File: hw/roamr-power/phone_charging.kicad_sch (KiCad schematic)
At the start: 0 parts

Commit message: reorganizing to roamr-power
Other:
- title: (none) -> ROAMR power board
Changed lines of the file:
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@@
 	(generator_version "9.0")
 	(paper "USLetter")
+	(title_block
+		(title "ROAMR power board")
+		(date "2026-01-18")
+		(rev "1.0")
+	)
 	(text "current limiter load switch here"
 		(exclude_from_sim no)

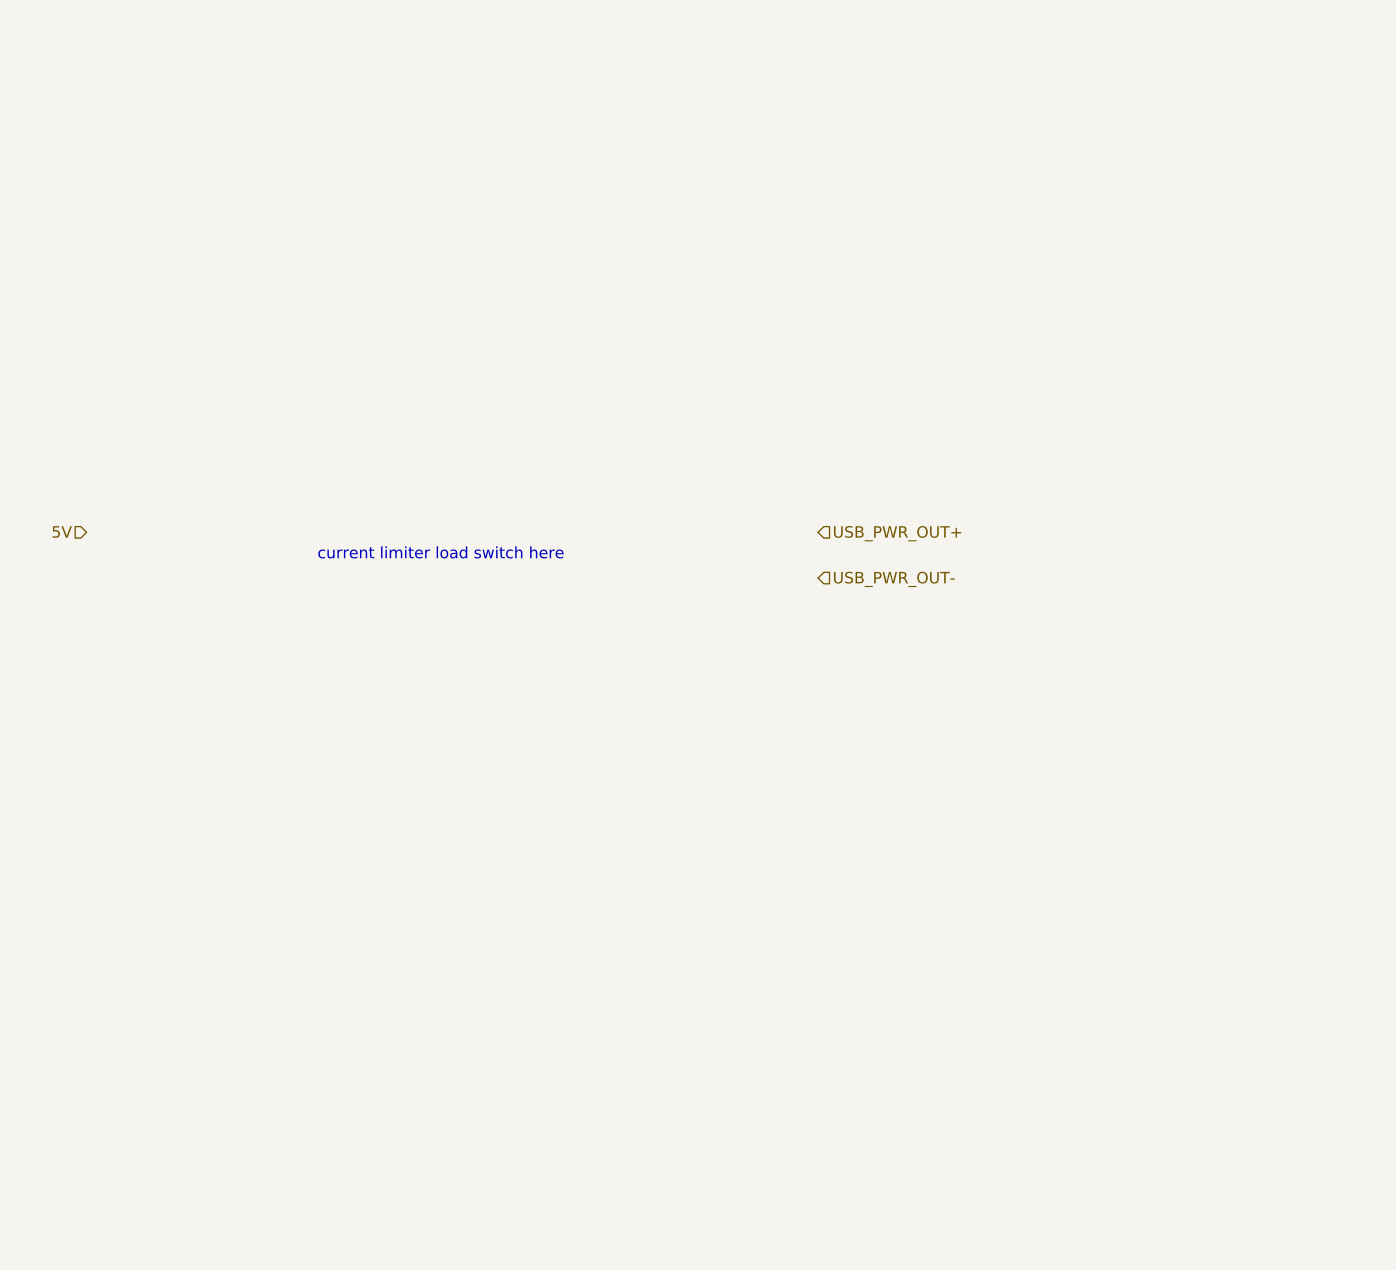
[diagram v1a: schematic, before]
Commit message: mostly finished power, probably need a bit of drawing cleanup, for schematic
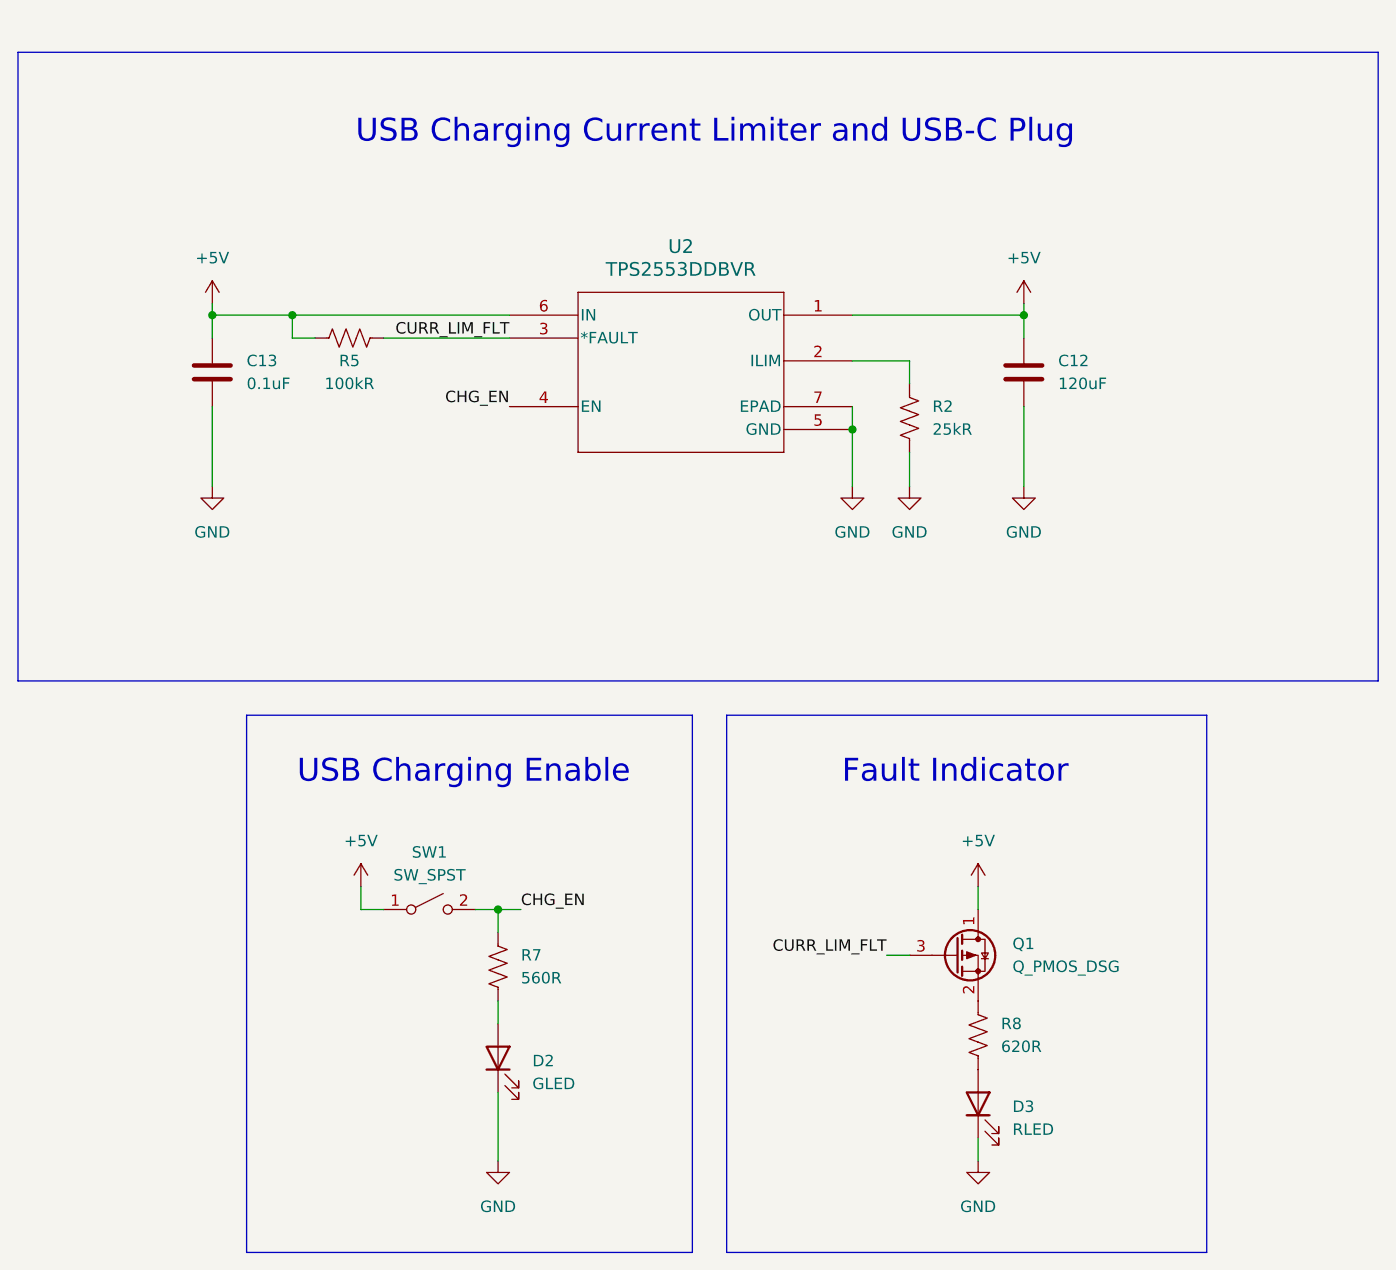
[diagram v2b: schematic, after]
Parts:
- added C12: 120uF, symbol Device:C
- added C13: 0.1uF, symbol Device:C
- added D2: GLED, symbol Device:LED
- added D3: RLED, symbol Device:LED
- added Q1: Q_PMOS_DSG, symbol Transistor_FET:Q_PMOS_DSG
- added R2: 25kR, symbol Device:R_US
- added R5: 100kR, symbol Device:R_US
- added R7: 560R, symbol Device:R_US
- added R8: 620R, symbol Device:R_US
- added SW1: SW_SPST, symbol Switch:SW_SPST
- added U2: TPS2553DDBVR, DRV6_1P6X1_TEX, symbol TPS2553DDBVR:TPS2553DDBVR
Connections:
- new net: R2.1, U2.2 (ILIM)
- new net: D2.2 (A), R7.2
- new net: Q1.2 (S), R8.1
- new net: D3.2 (A), R8.2
- new net +5V: C12.1, C13.1, Q1.1 (D), R5.1, SW1.1 (A), U2.1 (OUT), U2.6 (IN)
- new net CHG_EN: R7.1, SW1.2 (B), U2.4 (EN)
- new net CURR_LIM_FLT: Q1.3 (G), R5.2, U2.3 (*FAULT)
- new net GND: C12.2, C13.2, D2.1 (K), D3.1 (K), R2.2, U2.5 (GND), U2.7 (EPAD)
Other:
- note added: "Fault Indicator"
- note added: "USB Charging Current Limiter and USB-C Plug"
- note added: "USB Charging Enable"
- note removed: "current limiter load switch here"

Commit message: fixed after nathan's rereview
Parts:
- removed C12: 120uF, symbol Device:C
- removed R5: 100kR, symbol Device:R_US
- added C12: 120uF, symbol Device:C_Polarized
- added C14: 0.1uF, symbol Device:C
- added R9: 100kR, symbol Device:R_US
- R2: value 25kR -> 24kR
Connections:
- net +5V: no longer Q1.1 (D), U2.1 (OUT)
- net CHG_EN: now also Q1.1 (D), R9.1; no longer U2.4 (EN)
- net GND: now also C12.2, C14.2
- net CURR_LIM_FLT renamed CURR_LIM_nFLT
- net CURR_LIM_nFLT: now also U2.4 (EN), C14.1, R9.2
- new net VCTRL_5V: C12.1, U2.1 (OUT)
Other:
- note added: "USB Charging Current Limiter"
- note removed: "USB Charging Current Limiter and USB-C Plug"
- company: (none) -> Mechatronics FYDP Group 16
- moved on the sheet: C13, D2, D3, Q1, R2, R7, R8, SW1

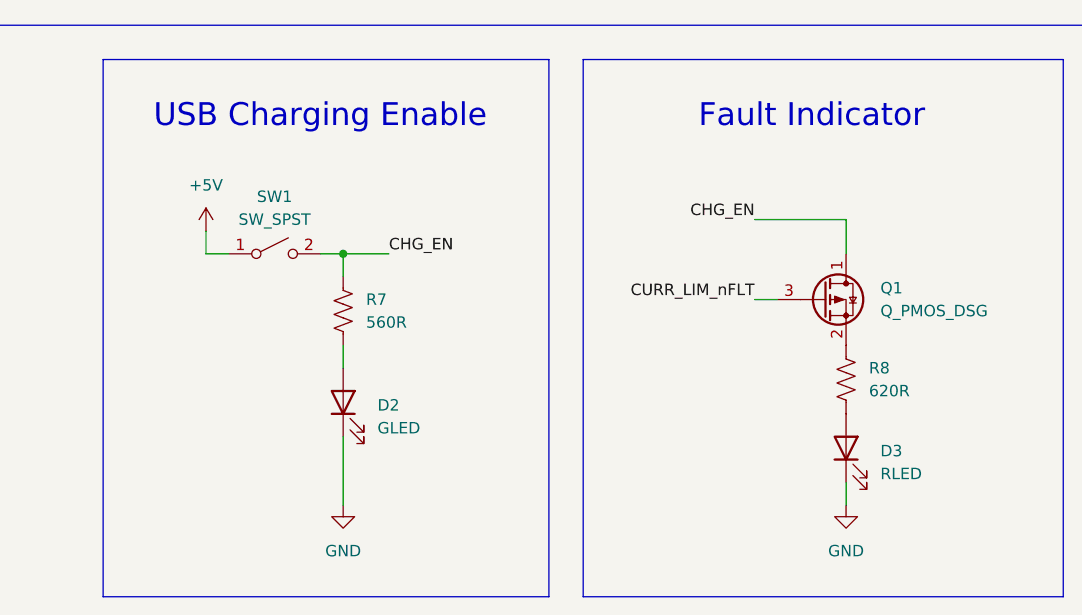
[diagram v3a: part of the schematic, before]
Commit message: picked the BOM and added two more indicator LEDs for the 12V and 5V rails
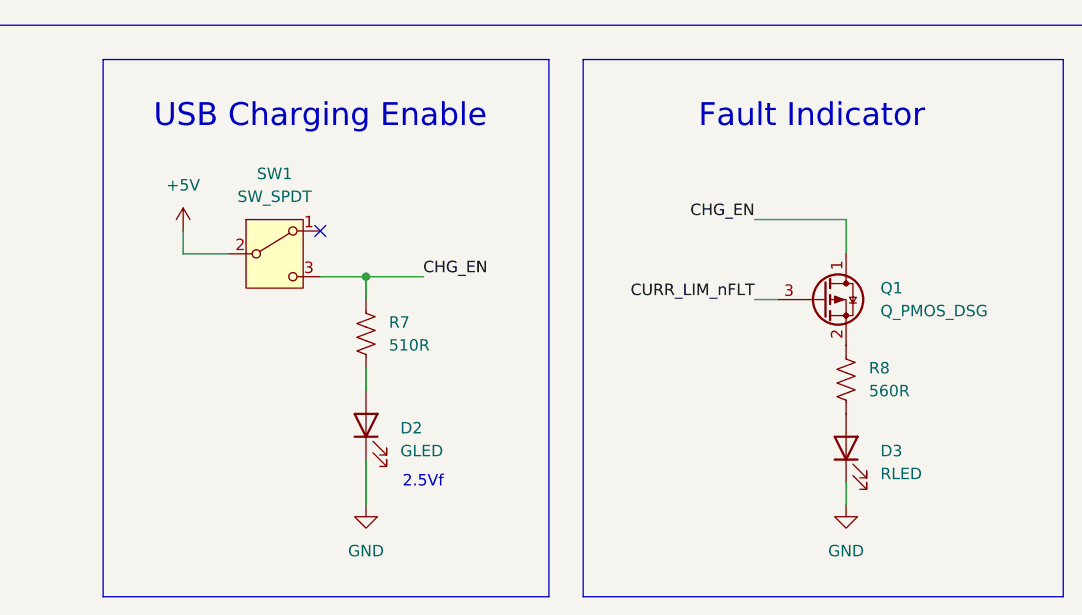
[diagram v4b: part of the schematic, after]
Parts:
- removed SW1: SW_SPST, symbol Switch:SW_SPST
- added SW1: SW_SPDT, OS102011MS2QN1:OS102011MA1QN1, symbol Switch:SW_SPDT
- C12: footprint (none) -> GYG1E121MCQ1GS:CAPAE660X610N
- C13, C14: footprint (none) -> Capacitor_SMD:C_0603_1608Metric
- D2: footprint (none) -> KT_EELP41.12-S2U1-25-2X4X-5-R18:KTEELP4112S2U1252X4X5R18
- D3: footprint (none) -> KR_DELPS1.22-VGVI-23-H3Q4:KRDELPS122VGVI23H3Q4
- Q1: footprint (none) -> BSS84PH6327XTSA2:SOT95P240X110-3N
- R2, R9: footprint (none) -> Resistor_SMD:R_0603_1608Metric
- R7: value 560R -> 510R; footprint (none) -> Resistor_SMD:R_0603_1608Metric
- R8: value 620R -> 560R; footprint (none) -> Resistor_SMD:R_0603_1608Metric
- U2: footprint DRV6_1P6X1_TEX -> TPS2553DDBVR:DRV6_1P6X1_TEX
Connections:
- net +5V: now also SW1.2 (B)
- net CHG_EN: now also SW1.3 (C)
- no-connect marks 0 -> 1
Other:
- note added: "2.5Vf"
- moved on the sheet: D2, R7

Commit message: layout
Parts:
- U2: footprint TPS2553DDBVR:DRV6_1P6X1_TEX -> TPS2553DDBVR:SOT95P280X145-6N
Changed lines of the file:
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@@
 			)
 		)
-		(property "Footprint" "TPS2553DDBVR:DRV6_1P6X1_TEX"
+		(property "Footprint" "TPS2553DDBVR:SOT95P280X145-6N"
 			(at 160.02 60.96 0)
 			(effects
@@
 		(on_board yes)
 		(dnp no)
-		(fields_autoplaced yes)
 		(property "Reference" "Q1"
-			(at 175.26 128.2699 0)
+			(at 175.26 129.54 0)
 			(effects
 				(font
@@
 				)
 				(justify left)
-			)
-		)
+				(hide yes)
+			)
+		)

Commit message: pcb schematic and layout updated
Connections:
- net +5V renamed VSYS_5V
- net VCTRL_5V renamed VLIM_5V
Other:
- note added: "Configured for 1A limit"
- moved on the sheet: C12, C13, C14, D2, D3, Q1, R2, R7, R8, R9, SW1, U2

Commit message: final changes
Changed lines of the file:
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@@
+	)
+	(junction
+		(at 166.37 54.61)
+		(diameter 0)
+		(color 0 0 0 0)
 	)
 	(junction
@@
 	(wire
 		(pts
+			(xy 166.37 54.61) (xy 179.07 54.61)
+		)
+		(stroke
+			(width 0)
+			(type default)
+		)
+	)
+	(wire
+		(pts
 			(xy 165.1 120.65) (xy 175.26 120.65)
 		)
@@
 	(wire
 		(pts
-			(xy 156.21 54.61) (xy 179.07 54.61)
+			(xy 156.21 54.61) (xy 166.37 54.61)
 		)
 		(stroke
@@
 					(unit 1)
 				)
+			)
+		)
+	)
+	(symbol
+		(lib_id "power:PWR_FLAG")
+		(at 166.37 54.61 0)
+		(unit 1)
+		(exclude_from_sim no)
+		(in_bom yes)
+		(on_board yes)
+		(dnp no)
+		(fields_autoplaced yes)
+		(property "Reference" "#FLG07"
+			(at 166.37 52.705 0)
+			(effects
+				(font
+					(size 1.27 1.27)
+				)
+				(hide yes)
+			)
+		)
+		(property "Value" "PWR_FLAG"
+			(at 166.37 49.53 0)
+			(effects
+				(font
+					(size 1.27 1.27)
+				)
+			)
+		)
+		(property "Footprint" ""
+			(at 166.37 54.61 0)
+			(effects
+				(font
+					(size 1.27 1.27)
+				)
+				(hide yes)
+			)
+		)
+		(property "Datasheet" "~"
+			(at 166.37 54.61 0)
+			(effects
+				(font
+					(size 1.27 1.27)
+				)
+				(hide yes)
+			)
+		)
+		(property "Description" "Special symbol for telling ERC where power comes from"
+			(at 166.37 54.61 0)
+			(effects
+				(font
+					(size 1.27 1.27)
+				)
+				(hide yes)
+			)
+		)
+		(pin "1"
+		)
+		(instances
+			(project "roamr-power"
+				(path "/bfe84b16-3df2-48dd-882e-523c3a68f778/7cadbd84-e43d-43ba-a052-9e62bf6faf2f"
+					(reference "#FLG07")
+					(unit 1)
+				)
